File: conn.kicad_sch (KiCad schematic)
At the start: 59 parts

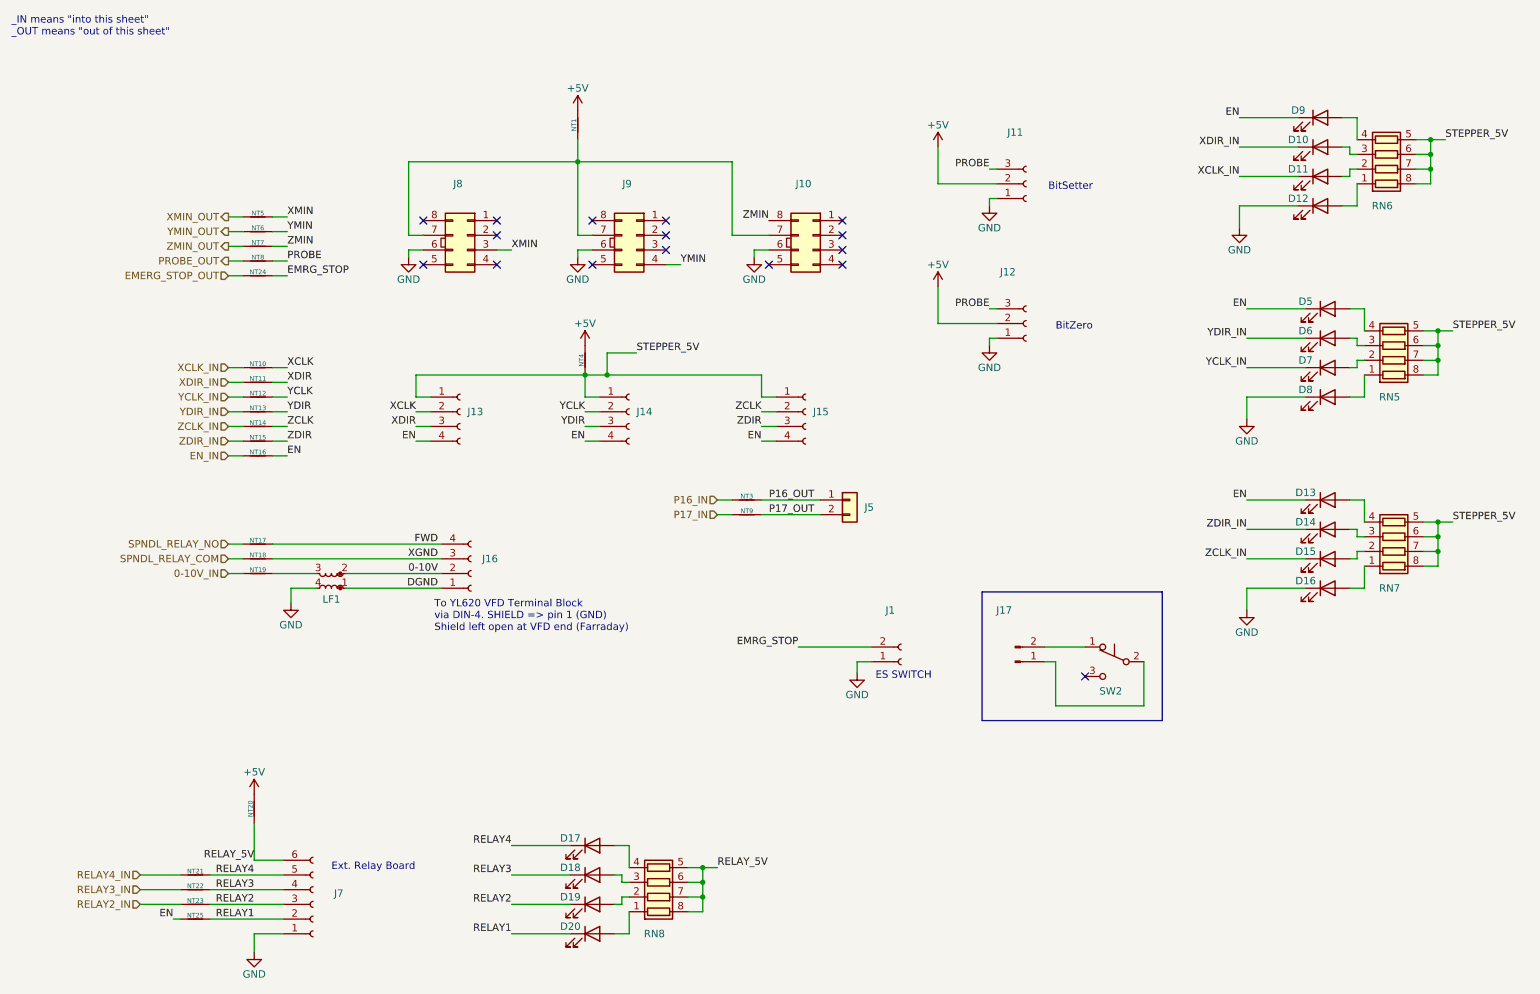
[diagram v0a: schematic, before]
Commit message: Removed 'Element14' field from all sch/pcb components
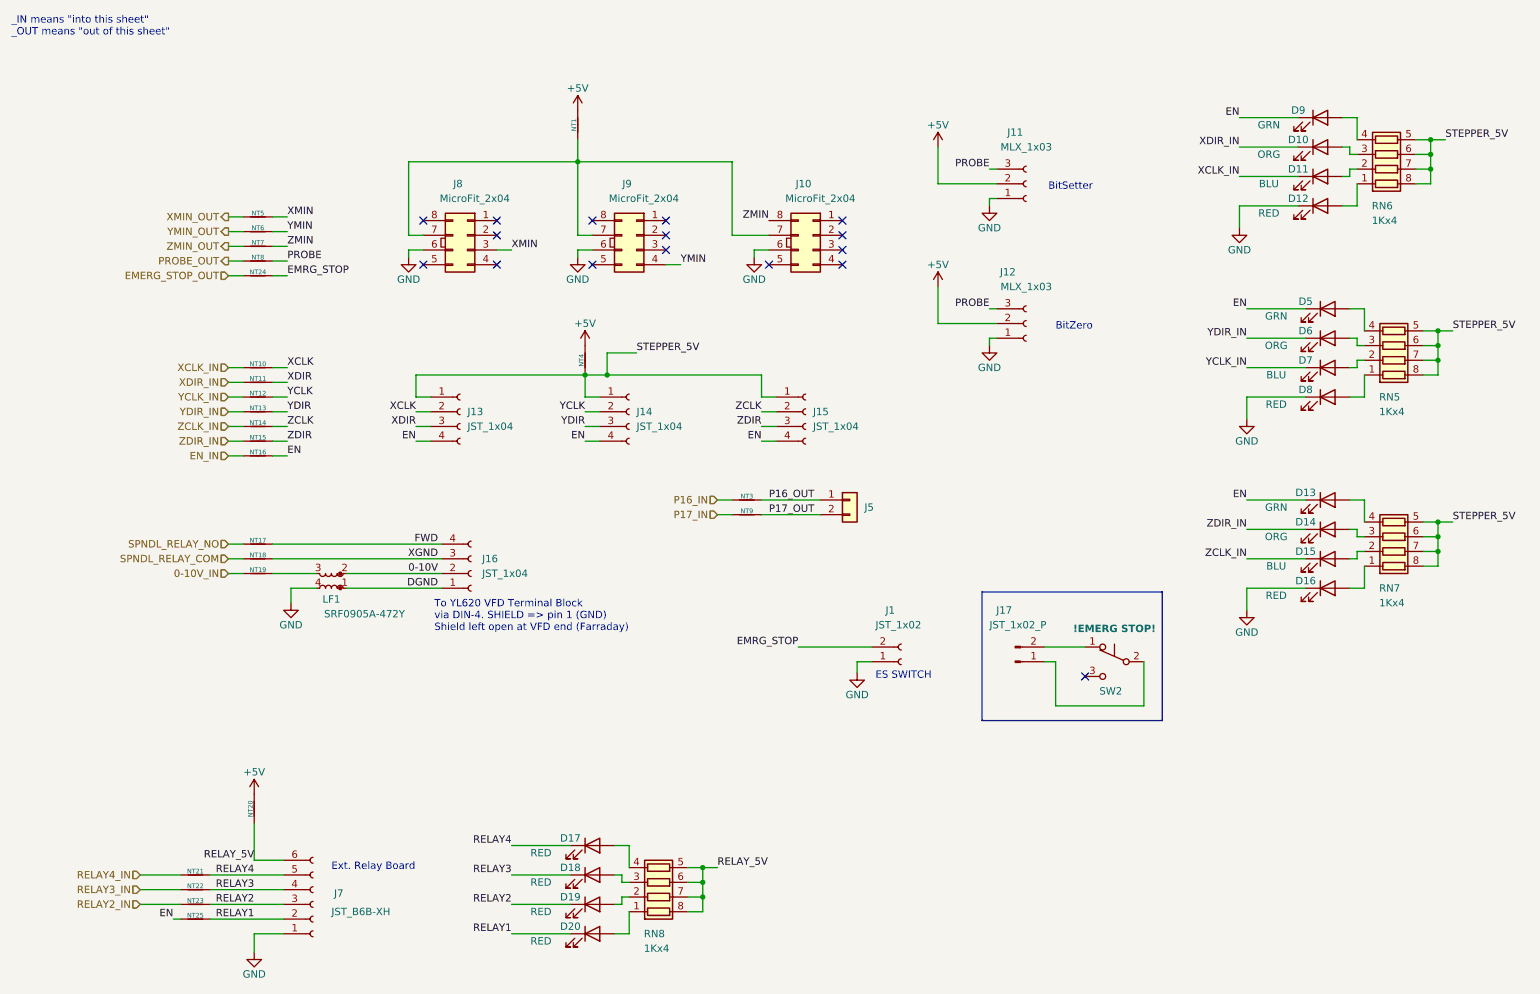
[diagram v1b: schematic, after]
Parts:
- D10, D14, D6: value (none) -> ORG; footprint (none) -> LED_SMD:LED_0402_1005Metric
- D11, D15, D7: value (none) -> BLU; footprint (none) -> LED_SMD:LED_0402_1005Metric
- D12, D16, D17, D18, D19, D20, D8: value (none) -> RED; footprint (none) -> LED_SMD:LED_0402_1005Metric
- D13, D5, D9: value (none) -> GRN; footprint (none) -> LED_SMD:LED_0402_1005Metric
- J1: value (none) -> JST_1x02; footprint (none) -> Connector_JST:JST_EH_S2B-EH_1x02_P2.50mm_Horizontal
- J10, J8, J9: value (none) -> MicroFit_2x04; footprint (none) -> Connector_Molex:Molex_Micro-Fit_3.0_43045-0812_2x04_P3.00mm_Vertical
- J11, J12: value (none) -> MLX_1x03; footprint (none) -> Connector_Molex:Molex_KK-254_AE-6410-03A_1x03_P2.54mm_Vertical
- J13, J14, J15, J16: value (none) -> JST_1x04; footprint (none) -> Connector_JST:JST_EH_S4B-EH_1x04_P2.50mm_Horizontal
- J17: value (none) -> JST_1x02_P
- J5: value (none) -> JST_01x02; footprint (none) -> Connector_JST:JST_EH_B2B-EH-A_1x02_P2.50mm_Vertical
- J7: value (none) -> JST_B6B-XH; footprint (none) -> Connector_JST:JST_EH_S6B-EH_1x06_P2.50mm_Horizontal
- LF1: value (none) -> SRF0905A-472Y; footprint (none) -> Filter:Filter_Bourns_SRF0905_6.0x9.2mm
- NT1, NT20, NT4: value (none) -> DNI; footprint (none) -> _footprints:NetTie-2_SMD_Pad1.0mm
- NT10, NT11, NT12, NT13, NT14, NT15, NT16, NT17, NT18, NT19, NT21, NT22, NT23, NT24, NT25, NT3, NT5, NT6, NT7, NT8, NT9: value (none) -> DNI; footprint (none) -> _footprints:NetTie-2_SMD_Pad0.3mm
- RN5, RN6, RN7, RN8: value (none) -> 1Kx4; footprint (none) -> Resistor_SMD:R_Array_Convex_4x0603
- SW2: value (none) -> !EMERG STOP!

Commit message: Reworked PSU control scheme (schematic only.)
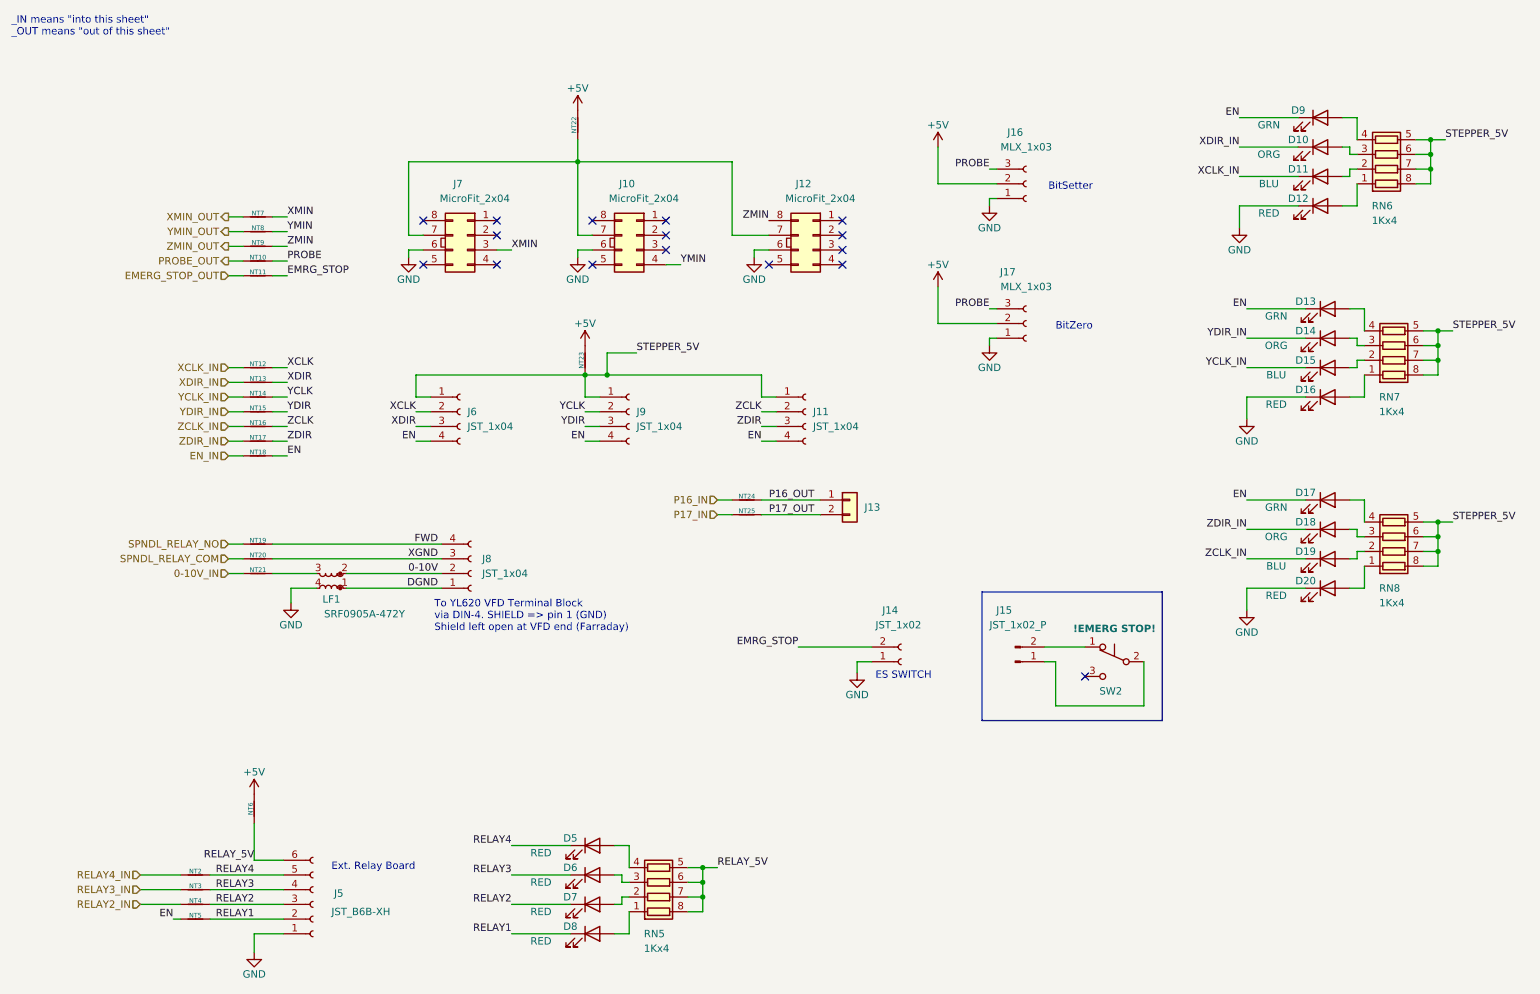
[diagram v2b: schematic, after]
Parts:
- renumbered D5 to D13, D6 to D14, D7 to D15, D8 to D16, D13 to D17, D14 to D18, D15 to D19, D16 to D20, D17 to D5, D18 to D6, D19 to D7, D20 to D8, J9 to J10, J15 to J11, J10 to J12, J5 to J13, J1 to J14, J17 to J15, J11 to J16, J12 to J17, J7 to J5, J13 to J6, J8 to J7, J16 to J8, J14 to J9, NT8 to NT10, NT24 to NT11, NT10 to NT12, NT11 to NT13, NT12 to NT14, NT13 to NT15, NT14 to NT16, NT15 to NT17, NT16 to NT18, NT17 to NT19, NT21 to NT2, NT18 to NT20, NT19 to NT21, NT1 to NT22, NT4 to NT23, NT3 to NT24, NT9 to NT25, NT22 to NT3, NT23 to NT4, NT25 to NT5, NT20 to NT6, NT5 to NT7, NT6 to NT8, NT7 to NT9, RN8 to RN5, RN5 to RN7, RN7 to RN8

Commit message: Change share/_footprints to share/module with new alias '-Project'
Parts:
- NT10, NT11, NT12, NT13, NT14, NT15, NT16, NT17, NT18, NT19, NT2, NT20, NT21, NT24, NT25, NT3, NT4, NT5, NT7, NT8, NT9: footprint _footprints:NetTie-2_SMD_Pad0.3mm -> -ProjectNetTie-2_SMD_Pad0.3mm
- NT22, NT23, NT6: footprint _footprints:NetTie-2_SMD_Pad1.0mm -> -ProjectNetTie-2_SMD_Pad1.0mm
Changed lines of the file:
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@@
       (effects (font (size 1.27 1.27)) hide)
     )
-    (property "Footprint" "_footprints:NetTie-2_SMD_Pad0.3mm" (id 2) (at 146.05 100.33 0)
+    (property "Footprint" "-ProjectNetTie-2_SMD_Pad0.3mm" (id 2) (at 146.05 100.33 0)
       (effects (font (size 1.27 1.27)) hide)
     )
@@
       (effects (font (size 1.27 1.27)) hide)
     )
-    (property "Footprint" "_footprints:NetTie-2_SMD_Pad0.3mm" (id 2) (at 50.8 172.72 0)
+    (property "Footprint" "-ProjectNetTie-2_SMD_Pad0.3mm" (id 2) (at 50.8 172.72 0)
       (effects (font (size 1.27 1.27)) hide)
     )
@@
       (effects (font (size 1.27 1.27)) hide)
     )
-    (property "Footprint" "_footprints:NetTie-2_SMD_Pad0.3mm" (id 2) (at 61.595 51.435 0)
+    (property "Footprint" "-ProjectNetTie-2_SMD_Pad0.3mm" (id 2) (at 61.595 51.435 0)
       (effects (font (size 1.27 1.27)) hide)
     )
@@
       (effects (font (size 1.27 1.27)) hide)
     )
-    (property "Footprint" "_footprints:NetTie-2_SMD_Pad0.3mm" (id 2) (at 50.8 170.18 0)
+    (property "Footprint" "-ProjectNetTie-2_SMD_Pad0.3mm" (id 2) (at 50.8 170.18 0)
       (effects (font (size 1.27 1.27)) hide)
     )
@@
       (effects (font (size 1.27 1.27)) hide)
     )
-    (property "Footprint" "_footprints:NetTie-2_SMD_Pad1.0mm" (id 2) (at 118.11 76.2 0)
+    (property "Footprint" "-ProjectNetTie-2_SMD_Pad1.0mm" (id 2) (at 118.11 76.2 0)
       (effects (font (size 1.27 1.27)) hide)
     )
@@
       (effects (font (size 1.27 1.27)) hide)
     )
-    (property "Footprint" "_footprints:NetTie-2_SMD_Pad0.3mm" (id 2) (at 61.595 77.47 0)
+    (property "Footprint" "-ProjectNetTie-2_SMD_Pad0.3mm" (id 2) (at 61.595 77.47 0)
       (effects (font (size 1.27 1.27)) hide)
     )
@@
       (effects (font (size 1.27 1.27)) hide)
     )
-    (property "Footprint" "_footprints:NetTie-2_SMD_Pad0.3mm" (id 2) (at 61.595 85.09 0)
+    (property "Footprint" "-ProjectNetTie-2_SMD_Pad0.3mm" (id 2) (at 61.595 85.09 0)
       (effects (font (size 1.27 1.27)) hide)
     )
@@
       (effects (font (size 1.27 1.27)) hide)
     )
-    (property "Footprint" "_footprints:NetTie-2_SMD_Pad0.3mm" (id 2) (at 50.8 167.64 0)
+    (property "Footprint" "-ProjectNetTie-2_SMD_Pad0.3mm" (id 2) (at 50.8 167.64 0)
       (effects (font (size 1.27 1.27)) hide)
     )
@@
       (effects (font (size 1.27 1.27)) hide)
     )
-    (property "Footprint" "_footprints:NetTie-2_SMD_Pad0.3mm" (id 2) (at 50.8 165.1 0)
+    (property "Footprint" "-ProjectNetTie-2_SMD_Pad0.3mm" (id 2) (at 50.8 165.1 0)
       (effects (font (size 1.27 1.27)) hide)
     )
@@
       (effects (font (size 1.27 1.27)) hide)
     )
-    (property "Footprint" "_footprints:NetTie-2_SMD_Pad0.3mm" (id 2) (at 61.595 92.71 0)
+    (property "Footprint" "-ProjectNetTie-2_SMD_Pad0.3mm" (id 2) (at 61.595 92.71 0)
       (effects (font (size 1.27 1.27)) hide)
     )
@@
       (effects (font (size 1.27 1.27)) hide)
     )
-    (property "Footprint" "_footprints:NetTie-2_SMD_Pad1.0mm" (id 2) (at 60.96 153.67 0)
+    (property "Footprint" "-ProjectNetTie-2_SMD_Pad1.0mm" (id 2) (at 60.96 153.67 0)
       (effects (font (size 1.27 1.27)) hide)
     )
@@
       (effects (font (size 1.27 1.27)) hide)
     )
-    (property "Footprint" "_footprints:NetTie-2_SMD_Pad0.3mm" (id 2) (at 61.595 87.63 0)
+    (property "Footprint" "-ProjectNetTie-2_SMD_Pad0.3mm" (id 2) (at 61.595 87.63 0)
       (effects (font (size 1.27 1.27)) hide)
     )
@@
       (effects (font (size 1.27 1.27)) hide)
     )
-    (property "Footprint" "_footprints:NetTie-2_SMD_Pad0.3mm" (id 2) (at 61.595 80.01 0)
+    (property "Footprint" "-ProjectNetTie-2_SMD_Pad0.3mm" (id 2) (at 61.595 80.01 0)
       (effects (font (size 1.27 1.27)) hide)
     )
@@
       (effects (font (size 1.27 1.27)) hide)
     )
-    (property "Footprint" "_footprints:NetTie-2_SMD_Pad0.3mm" (id 2) (at 61.595 90.17 0)
+    (property "Footprint" "-ProjectNetTie-2_SMD_Pad0.3mm" (id 2) (at 61.595 90.17 0)
       (effects (font (size 1.27 1.27)) hide)
     )
@@
       (effects (font (size 1.27 1.27)) hide)
     )
-    (property "Footprint" "_footprints:NetTie-2_SMD_Pad0.3mm" (id 2) (at 61.595 59.055 0)
+    (property "Footprint" "-ProjectNetTie-2_SMD_Pad0.3mm" (id 2) (at 61.595 59.055 0)
       (effects (font (size 1.27 1.27)) hide)
     )
@@
       (effects (font (size 1.27 1.27)) hide)
     )
-    (property "Footprint" "_footprints:NetTie-2_SMD_Pad0.3mm" (id 2) (at 146.05 102.87 0)
+    (property "Footprint" "-ProjectNetTie-2_SMD_Pad0.3mm" (id 2) (at 146.05 102.87 0)
       (effects (font (size 1.27 1.27)) hide)
     )
@@
       (effects (font (size 1.27 1.27)) hide)
     )
-    (property "Footprint" "_footprints:NetTie-2_SMD_Pad0.3mm" (id 2) (at 61.595 53.975 0)
+    (property "Footprint" "-ProjectNetTie-2_SMD_Pad0.3mm" (id 2) (at 61.595 53.975 0)
       (effects (font (size 1.27 1.27)) hide)
     )
@@
       (effects (font (size 1.27 1.27)) hide)
     )
-    (property "Footprint" "_footprints:NetTie-2_SMD_Pad1.0mm" (id 2) (at 116.84 35.56 0)
+    (property "Footprint" "-ProjectNetTie-2_SMD_Pad1.0mm" (id 2) (at 116.84 35.56 0)
       (effects (font (size 1.27 1.27)) hide)
     )
@@
       (effects (font (size 1.27 1.27)) hide)
     )
-    (property "Footprint" "_footprints:NetTie-2_SMD_Pad0.3mm" (id 2) (at 61.595 107.95 0)
+    (property "Footprint" "-ProjectNetTie-2_SMD_Pad0.3mm" (id 2) (at 61.595 107.95 0)
       (effects (font (size 1.27 1.27)) hide)
     )
@@
       (effects (font (size 1.27 1.27)) hide)
     )
-    (property "Footprint" "_footprints:NetTie-2_SMD_Pad0.3mm" (id 2) (at 61.595 113.03 0)
+    (property "Footprint" "-ProjectNetTie-2_SMD_Pad0.3mm" (id 2) (at 61.595 113.03 0)
       (effects (font (size 1.27 1.27)) hide)
     )
@@
       (effects (font (size 1.27 1.27)) hide)
     )
-    (property "Footprint" "_footprints:NetTie-2_SMD_Pad0.3mm" (id 2) (at 61.595 110.49 0)
+    (property "Footprint" "-ProjectNetTie-2_SMD_Pad0.3mm" (id 2) (at 61.595 110.49 0)
       (effects (font (size 1.27 1.27)) hide)
     )
@@
       (effects (font (size 1.27 1.27)) hide)
     )
-    (property "Footprint" "_footprints:NetTie-2_SMD_Pad0.3mm" (id 2) (at 61.595 56.515 0)
+    (property "Footprint" "-ProjectNetTie-2_SMD_Pad0.3mm" (id 2) (at 61.595 56.515 0)
       (effects (font (size 1.27 1.27)) hide)
     )
@@
       (effects (font (size 1.27 1.27)) hide)
     )
-    (property "Footprint" "_footprints:NetTie-2_SMD_Pad0.3mm" (id 2) (at 61.595 61.595 0)
+    (property "Footprint" "-ProjectNetTie-2_SMD_Pad0.3mm" (id 2) (at 61.595 61.595 0)
       (effects (font (size 1.27 1.27)) hide)
     )
@@
       (effects (font (size 1.27 1.27)) hide)
     )
-    (property "Footprint" "_footprints:NetTie-2_SMD_Pad0.3mm" (id 2) (at 61.595 82.55 0)
-      (effects (font (size 1.27 1.27)) hide)
-    )
+    (property "Footprint" "-ProjectNetTie-2_SMD_Pad0.3mm" (id 2) (at 61.595 82.55 0)
+      (effects (font (size 1.27 1.27)) hide)
+    )
